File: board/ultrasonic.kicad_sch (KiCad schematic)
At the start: 21 parts, among them Q7 BSS123, Q8 BSS123, T1 B78416A2232A003, U8 PGA460TPWR

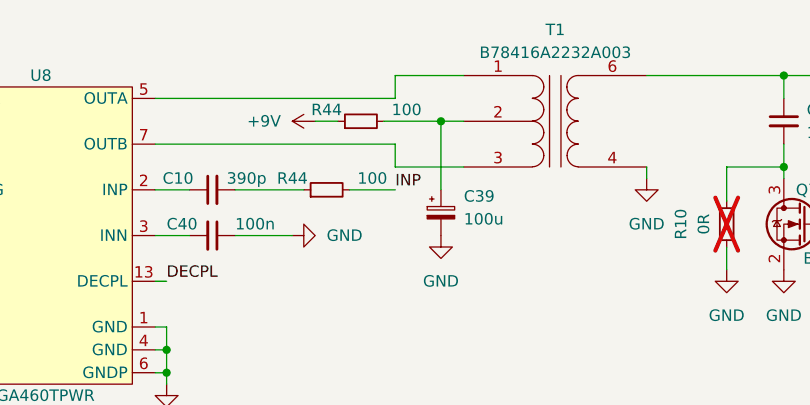
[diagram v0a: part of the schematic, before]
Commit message: Rough placement of US electronics
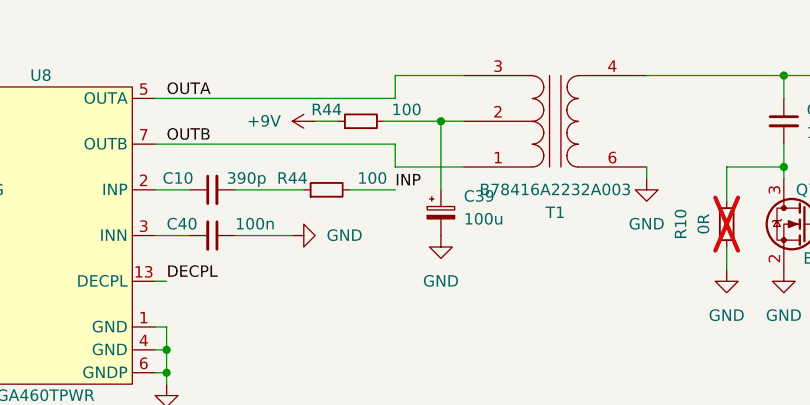
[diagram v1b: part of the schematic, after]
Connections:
- net GND: now also T1.6 (S2); no longer T1.4 (S1)
- net INP: now also T1.4 (S1); no longer T1.6 (S2)
- net OUTA: now reaches U8.5 (OUTA)
- net OUTA: now also T1.3 (PR2); no longer T1.1 (PR1)
- net OUTB: now reaches U8.7 (OUTB)
- net OUTB: now also T1.1 (PR1); no longer T1.3 (PR2)

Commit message: Routing basically finished
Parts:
- added R43: 10, Resistor_SMD:R_1206_3216Metric, symbol Device:R_Small
- R44: footprint Resistor_SMD:R_0603_1608Metric -> Resistor_SMD:R_1206_3216Metric; JLC_BasicPart yes -> no; JLC_PN C22775 -> C2934192; MPN 0603WAF1000T5E -> FRD1206J101 TS; Manufacturer UNI-ROYAL(Uniroyal Elec) -> FOJAN
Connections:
- net +9V: now also R43.1; no longer C34.1, U8.15 (VPWR)
- new net: C34.1, R43.2, U8.15 (VPWR)
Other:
- moved on the sheet: C34, C36, C37, C39

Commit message: Added beads, fixed a few part numbers, exported gerber/drill This is the ordered version
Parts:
- C39: JLC_PN C525872 -> C111600; MPN EMVY160ADA101MF55G -> UWX1C101MCL1GB; Manufacturer NCC(Nippon Chemi-Con) -> Nichicon
- R43: JLC_PN C4094378 -> C25349; MPN CRCW120610R0JNEBC -> 1206W4J0100T5E; Manufacturer Vishay Intertech -> UNI-ROYAL(Uniroyal Elec)
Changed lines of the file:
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@@
       (effects (font (size 1.27 1.27)) hide)
     )
-    (property "MPN" "EMVY160ADA101MF55G" (at 151.13 91.44 0)
+    (property "MPN" "UWX1C101MCL1GB" (at 151.13 91.44 0)
       (effects (font (size 1.27 1.27)) hide)
     )
@@
       (effects (font (size 1.27 1.27)) hide)
     )
-    (property "JLC_PN" "C525872" (at 151.13 91.44 0)
+    (property "JLC_PN" "C111600" (at 151.13 91.44 0)
       (effects (font (size 1.27 1.27)) hide)
     )
@@
       (effects (font (size 1.27 1.27)) hide)
     )
-    (property "Manufacturer" "NCC(Nippon Chemi-Con)" (at 151.13 91.44 0)
+    (property "Manufacturer" "Nichicon" (at 151.13 91.44 0)
       (effects (font (size 1.27 1.27)) hide)
     )
@@
       (effects (font (size 1.27 1.27)) hide)
     )
-    (property "MPN" "CRCW120610R0JNEBC" (at 90.17 71.12 0)
+    (property "MPN" "1206W4J0100T5E" (at 90.17 71.12 0)
       (effects (font (size 1.27 1.27)) hide)
     )
@@
       (effects (font (size 1.27 1.27)) hide)
     )
-    (property "JLC_PN" "C4094378" (at 90.17 71.12 0)
-      (effects (font (size 1.27 1.27)) hide)
-    )
-    (property "Manufacturer" "Vishay Intertech" (at 90.17 71.12 0)
-      (effects (font (size 1.27 1.27)) hide)
-    )
+    (property "JLC_PN" "C25349" (at 90.17 71.12 0)
+      (effects (font (size 1.27 1.27)) hide)
+    )
+    (property "Manufacturer" "UNI-ROYAL(Uniroyal Elec)" (at 90.17 71.12 0)
+      (effects (font (size 1.27 1.27)) hide)
+    )

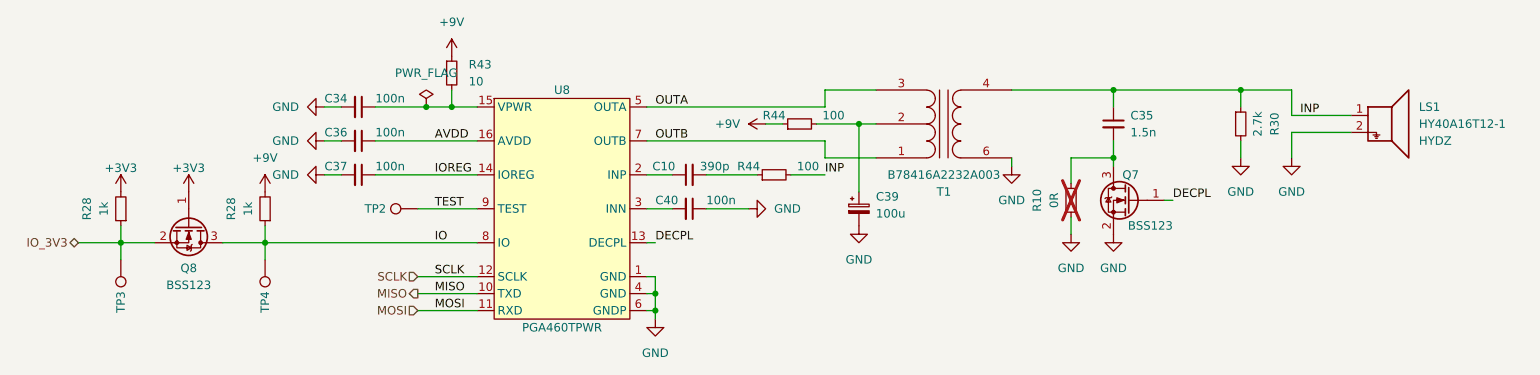
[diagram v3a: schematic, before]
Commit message: Fixed full errata, now v2.1 Most important changes: * Changed power supply architecture * Added hardware ID resistors * Moved USB connector closer to/over the border * Added a 2A fuse * Replaced Beads to display with resistors for better signal integrity * Replaced IP5306 with IP5303 for lower charging current * Switched PGA sensors from TCI to SPI, removed TCI/IO connection * Switched PGA mode from temperature to time decoupling * Added a power-on-reset circuit to keep power-consumption low due to voltage on 5V rail if turned off * Retracted copper planes from the PCB border * Added fabrication output using KiCAD JLCPCB tools
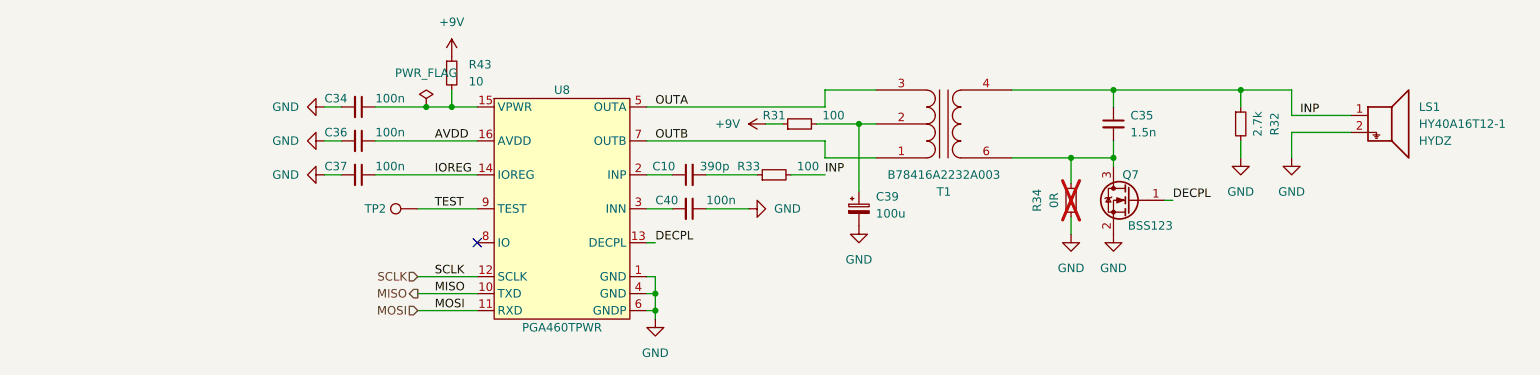
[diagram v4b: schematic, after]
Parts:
- removed Q8: BSS123, Package_TO_SOT_SMD:SOT-23, symbol Transistor_FET:BSS123
- removed R28 (x2): 1k, Resistor_SMD:R_0603_1608Metric, symbol Device:R_Small
- removed TP3, TP4: TestPoint, TestPoint:TestPoint_Pad_1.0x1.0mm, symbol Connector:TestPoint
- R43: JLC_BasicPart (none) -> no
- renumbered R44 to R31, R30 to R32, R44 to R33, R10 to R34
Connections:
- net GND: no longer T1.6 (S2)
- net at C35.2, Q7.3 (D), R34.2: now also T1.6 (S2)
- net IO: no longer names the net of U8.8 (IO)
- no-connect marks 0 -> 1

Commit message: Hardware Revision
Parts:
- renumbered C10 to C38

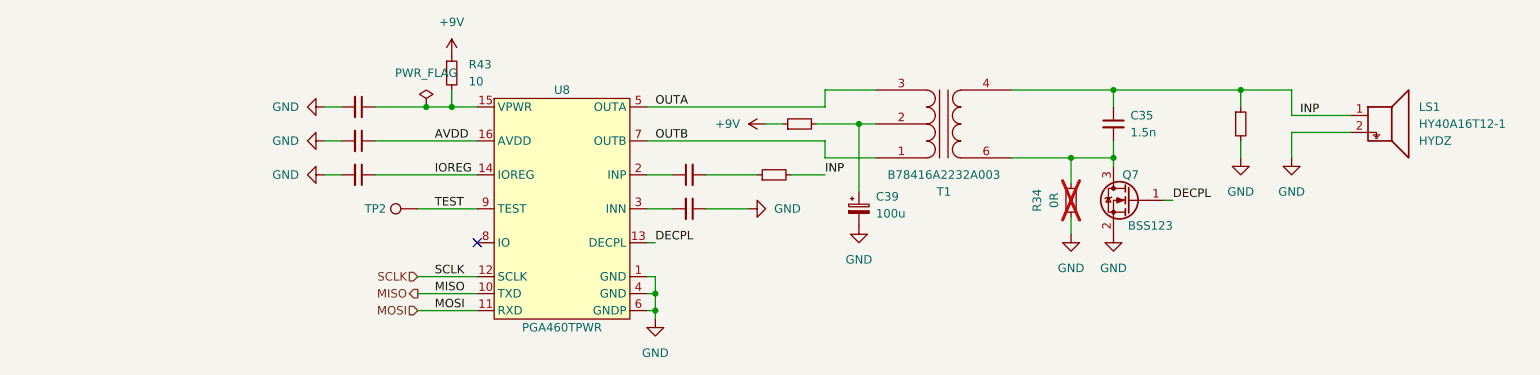
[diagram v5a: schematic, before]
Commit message: Fix errors in schematic for new board design
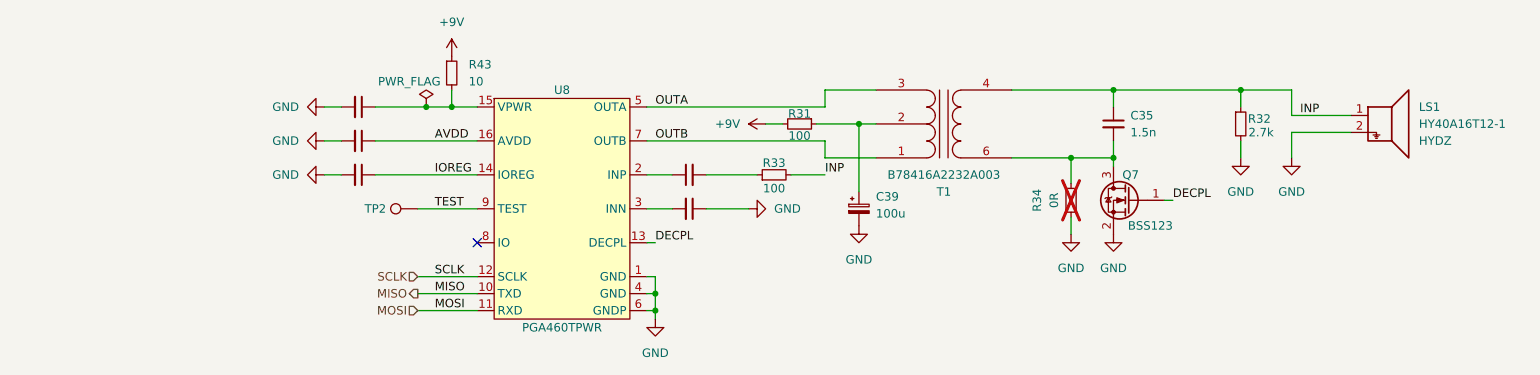
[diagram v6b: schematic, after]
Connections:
- net +9V: now also R31.2; no longer R31.1
- net at C39.1, T1.2 (PM): now also R31.1; no longer R31.2
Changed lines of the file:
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@@
 (kicad_sch
-	(version 20231120)
+	(version 20250114)
 	(generator "eeschema")
-	(generator_version "8.0")
+	(generator_version "9.0")
 	(paper "A4")
 	(junction
@@
 	(label "SCLK"
 		(at 87.63 101.6 0)
-		(fields_autoplaced yes)
 		(effects
 			(font
@@
 	(label "MOSI"
 		(at 87.63 106.68 0)
-		(fields_autoplaced yes)
 		(effects
 			(font
@@
 	(label "TEST"
 		(at 87.63 91.44 0)
-		(fields_autoplaced yes)
 		(effects
 			(font
@@
 	(label "OUTA"
 		(at 120.65 76.2 0)
-		(fields_autoplaced yes)
 		(effects
 			(font
@@
 	(label "OUTB"
 		(at 120.65 81.28 0)
-		(fields_autoplaced yes)
 		(effects
 			(font
@@
 	(label "AVDD"
 		(at 87.63 81.28 0)
-		(fields_autoplaced yes)
 		(effects
 			(font
@@
 	(label "DECPL"
 		(at 120.65 96.52 0)
-		(fields_autoplaced yes)
 		(effects
 			(font
@@
 	(label "INP"
 		(at 217.17 77.47 0)
-		(fields_autoplaced yes)
 		(effects
 			(font
@@
 	(label "INP"
 		(at 146.05 86.36 0)
-		(fields_autoplaced yes)
 		(effects
 			(font
@@
 	(label "MISO"
 		(at 87.63 104.14 0)
-		(fields_autoplaced yes)
 		(effects
 			(font
@@
 	(label "IOREG"
 		(at 87.63 86.36 0)
-		(fields_autoplaced yes)
 		(effects
 			(font
@@
 	(label "DECPL"
 		(at 198.12 90.17 0)
-		(fields_autoplaced yes)
 		(effects
 			(font
@@
 		(shape input)
 		(at 85.09 106.68 180)
-		(fields_autoplaced yes)
 		(effects
 			(font
@@
 		(shape output)
 		(at 85.09 104.14 180)
-		(fields_autoplaced yes)
 		(effects
 			(font
@@
 		(shape input)
 		(at 85.09 101.6 180)
-		(fields_autoplaced yes)
 		(effects
 			(font
@@
 		(on_board yes)
 		(dnp no)
-		(fields_autoplaced yes)
 		(property "Reference" "#FLG08"
 			(at 86.36 74.295 0)
@@
 		)
 		(property "Value" "PWR_FLAG"
-			(at 86.36 71.12 0)
+			(at 83.82 72.39 0)
 			(effects
 				(font
@@
 	(symbol
 		(lib_id "Device:R_Small")
-		(at 142.24 78.74 90)
+		(at 142.24 78.74 270)
 		(unit 1)
 		(exclude_from_sim no)
@@
 		(dnp no)
 		(property "Reference" "R31"
-			(at 142.24 78.74 0)
-			(effects
-				(font
-					(size 1.27 1.27)
-				)
-				(hide yes)
+			(at 142.24 77.216 90)
+			(effects
+				(font
+					(size 1.27 1.27)
+				)
 			)
 		)
 		(property "Value" "100"
-			(at 142.24 78.74 0)
-			(effects
-				(font
-					(size 1.27 1.27)
-				)
-				(hide yes)
+			(at 142.24 80.518 90)
+			(effects
+				(font
+					(size 1.27 1.27)
+				)
 			)
 		)
@@
 		(dnp no)
 		(property "Reference" "R33"
-			(at 138.43 86.36 0)
-			(effects
-				(font
-					(size 1.27 1.27)
-				)
-				(hide yes)
+			(at 138.43 84.582 90)
+			(effects
+				(font
+					(size 1.27 1.27)
+				)
 			)
 		)
 		(property "Value" "100"
-			(at 138.43 86.36 0)
-			(effects
-				(font
-					(size 1.27 1.27)
-				)
-				(hide yes)
+			(at 138.43 88.392 90)
+			(effects
+				(font
+					(size 1.27 1.27)
+				)
 			)
 		)
@@
 		(dnp no)
 		(property "Reference" "R32"
-			(at 208.28 78.74 0)
-			(effects
-				(font
-					(size 1.27 1.27)
-				)
-				(hide yes)
+			(at 211.074 77.978 0)
+			(effects
+				(font
+					(size 1.27 1.27)
+				)
 			)
 		)
 		(property "Value" "2.7k"
-			(at 208.28 78.74 0)
-			(effects
-				(font
-					(size 1.27 1.27)
-				)
-				(hide yes)
-			)
-		)
+			(at 211.328 80.01 0)
+			(effects
+				(font
+					(size 1.27 1.27)
+				)
+			)
+		)

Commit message: Schematic updates
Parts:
- R31: footprint Resistor_SMD:R_1206_3216Metric -> Resistor_SMD:R_0603_1608Metric; JLC_PN C2934192 -> C22775; MPN FRD1206J101 TS -> 0603WAF1000T5E; Manufacturer FOJAN -> UNI-ROYAL(Uniroyal Elec)
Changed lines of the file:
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@@
 			)
 		)
-		(property "Footprint" "Resistor_SMD:R_1206_3216Metric"
+		(property "Footprint" "Resistor_SMD:R_0603_1608Metric"
 			(at 142.24 78.74 0)
 			(effects
@@
 			)
 		)
-		(property "JLC_PN" "C2934192"
+		(property "JLC_PN" "C22775"
 			(at 142.24 78.74 0)
 			(effects
@@
 			)
 		)
-		(property "MPN" "FRD1206J101 TS"
+		(property "MPN" "0603WAF1000T5E"
 			(at 142.24 78.74 0)
 			(effects
@@
 			)
 		)
-		(property "Manufacturer" "FOJAN"
+		(property "Manufacturer" "UNI-ROYAL(Uniroyal Elec)"
 			(at 142.24 78.74 0)
 			(effects

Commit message: Update schematic and PCB layout
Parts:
- R43: footprint Resistor_SMD:R_1206_3216Metric -> Resistor_SMD:R_0603_1608Metric; JLC_PN C25349 -> C22859; MPN 1206W4J0100T5E -> 0603WAF100JT5E
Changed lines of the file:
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@@
 			)
 		)
-		(property "Footprint" "Resistor_SMD:R_1206_3216Metric"
+		(property "Footprint" "Resistor_SMD:R_0603_1608Metric"
 			(at 90.17 71.12 0)
 			(effects
@@
 			)
 		)
-		(property "MPN" "1206W4J0100T5E"
+		(property "MPN" "0603WAF100JT5E"
 			(at 90.17 71.12 0)
 			(effects
@@
 			)
 		)
-		(property "JLC_PN" "C25349"
+		(property "JLC_PN" "C22859"
 			(at 90.17 71.12 0)
 			(effects
